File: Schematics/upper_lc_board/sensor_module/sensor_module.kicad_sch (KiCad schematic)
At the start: 30 parts, among them J2 HAL_SENS, J3 PT, J4 PT2, J7 TC, U7 ADC_ADS131M04IPWR, U9 OA-TLV9001IDCK

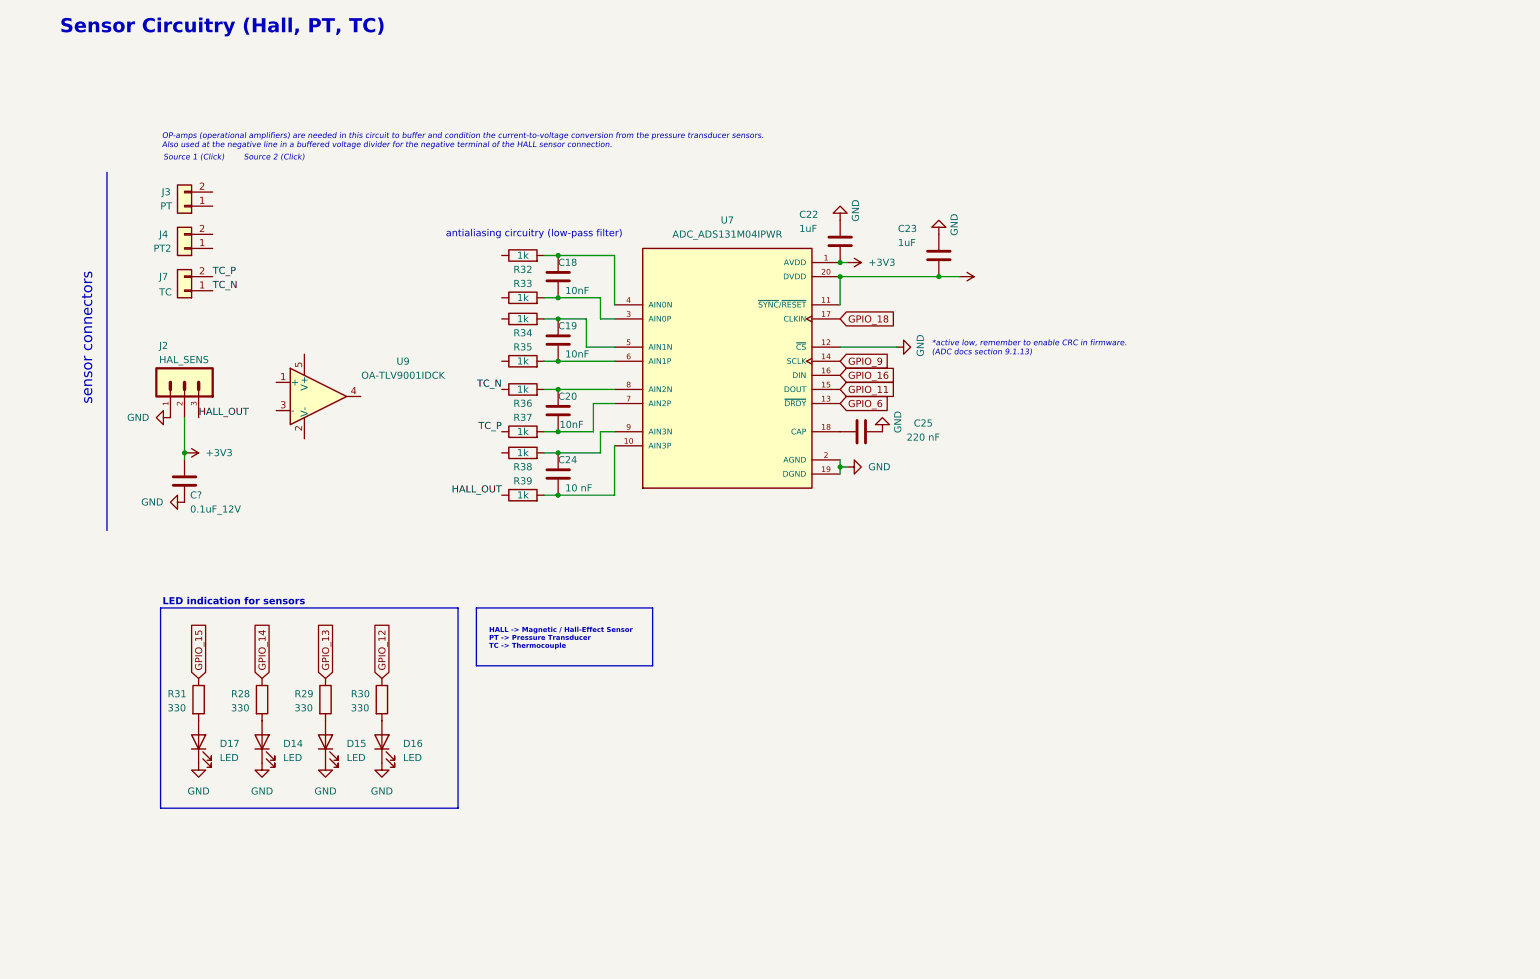
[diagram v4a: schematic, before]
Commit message: update sensor circuitry; implement reccomended pre-ADC circuitry
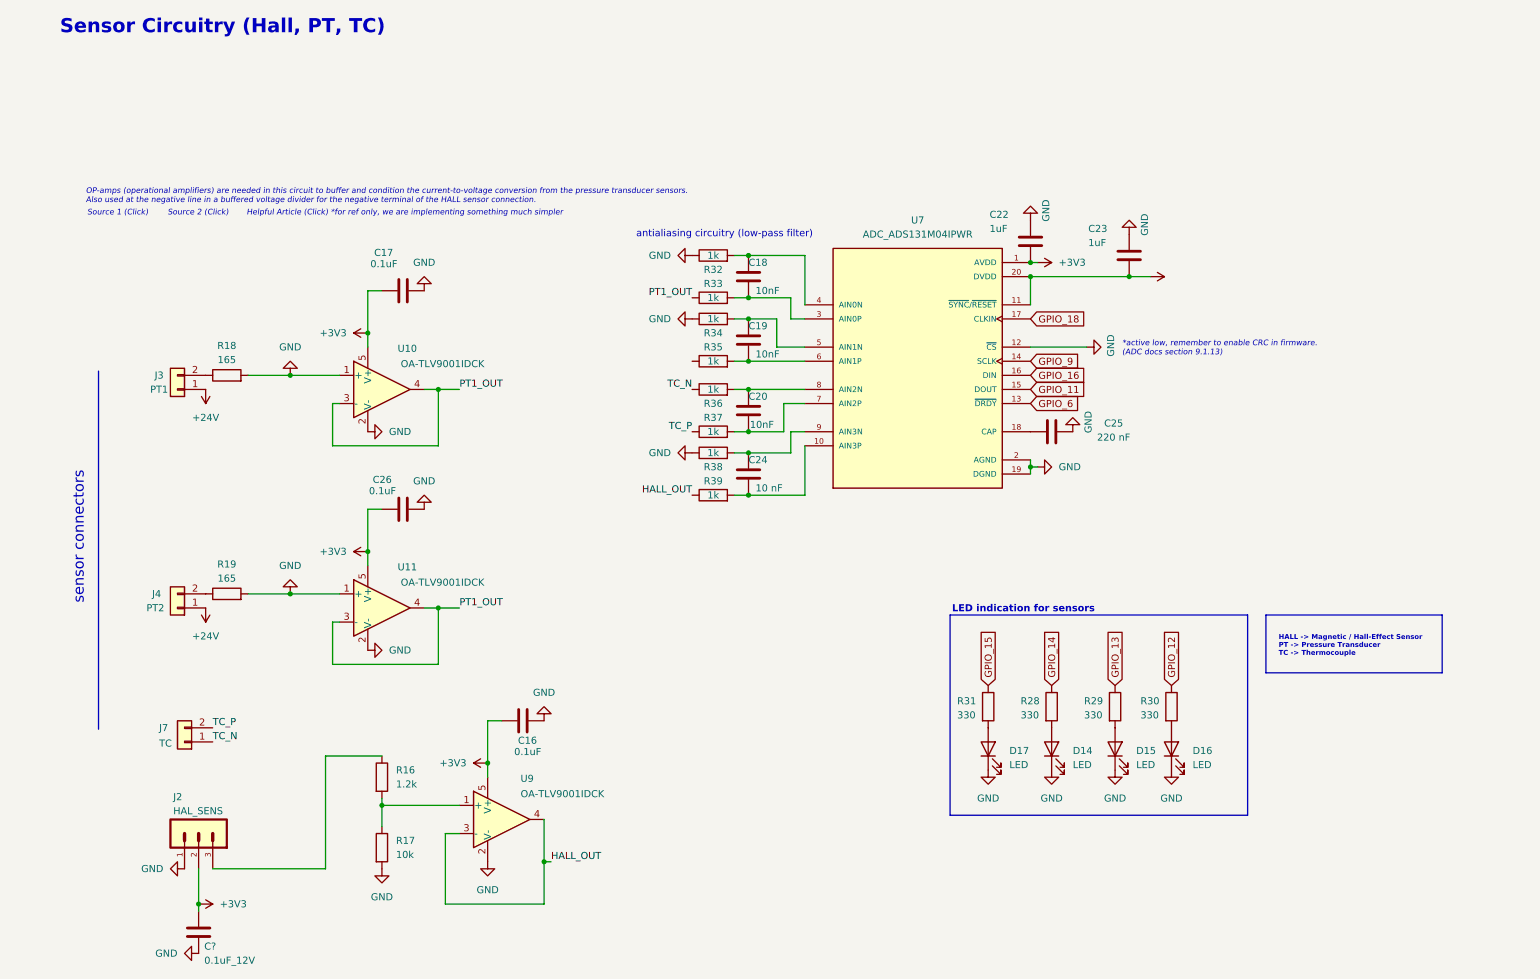
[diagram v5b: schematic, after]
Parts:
- added C16, C17, C26: 0.1uF, symbol Device:C
- added R16: 1.2k, symbol Device:R
- added R17: 10k, symbol Device:R
- added R18, R19: 165, symbol Device:R
- added U10, U11: OA-TLV9001IDCK, Package_TO_SOT_SMD:SOT-353_SC-70-5, symbol Amplifier_Operational:TLV9001IDCK
- J3: value PT -> PT1
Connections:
- net +3V3: now also U9.5 (V+), C16.1, C17.1, C26.1, U10.5 (V+), U11.5 (V+)
- net GND: now also R32.1, R34.1, R38.1, U9.2 (V-), C16.2, C17.2, C26.2, R17.2, R18.2, R19.2, U10.1 (+), U10.2 (V-), U11.1 (+), U11.2 (V-)
- net HALL_OUT: now also U9.3 (-), U9.4; no longer J2.3
- net +24V: now reaches J4.1 (Pin_1)
- net +24V: now also J3.1 (Pin_1)
- net at J4.2 (Pin_2): now also R19.1
- net at J3.2 (Pin_2): now also R18.1
- net at U9.1 (+): now also R16.2, R17.1
- net PT1_OUT: now reaches R33.1
- net PT1_OUT: now also U10.3 (-), U10.4, U11.3 (-), U11.4
- new net: J2.3, R16.1
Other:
- note added: "Helpful Article (Click) *for ref only, we are implementing something much simpler"
- moved on the sheet: C18, C19, C20, C22, C23, C24, C25, C?, D14, D15, D16, D17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

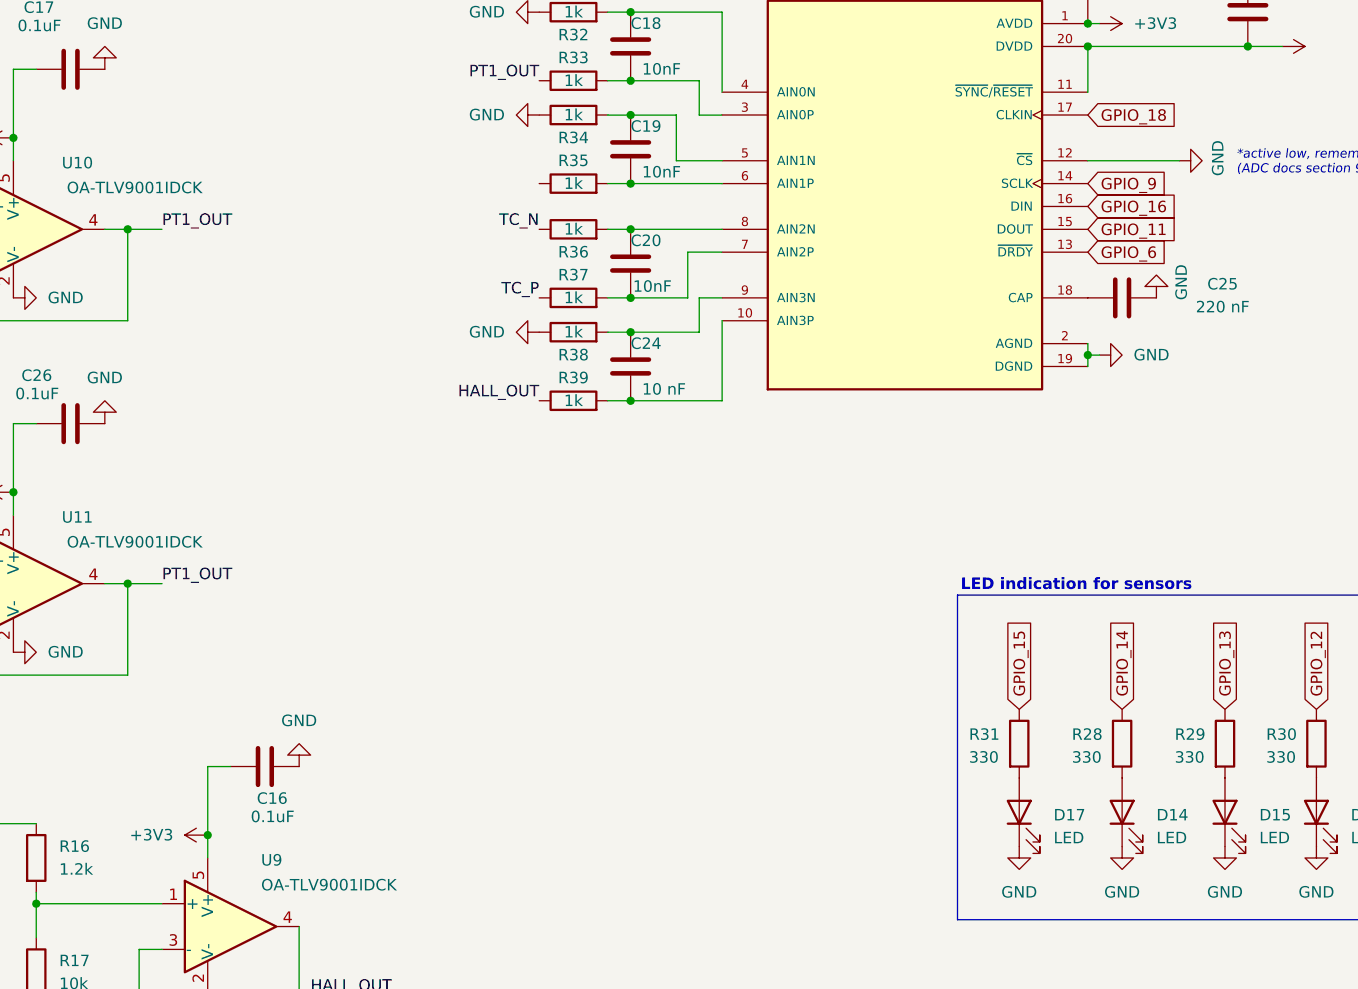
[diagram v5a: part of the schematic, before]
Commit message: update power circuitry (replaced OR-ing setup with a single power mux IC)
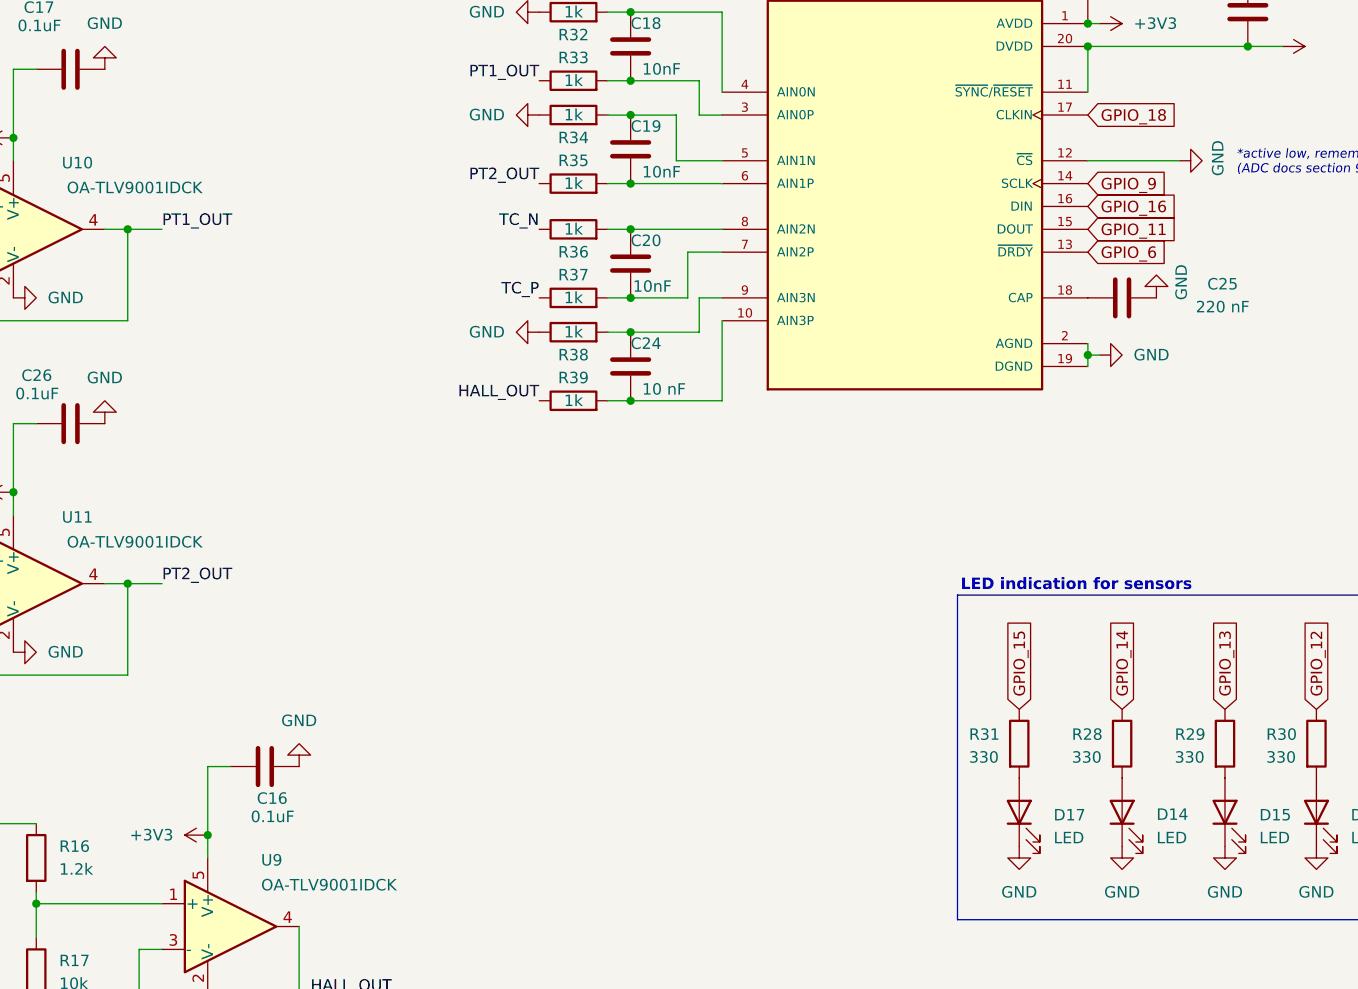
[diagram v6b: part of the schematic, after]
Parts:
- C16, C17, C18, C19, C20, C24, C26: footprint (none) -> Capacitor_SMD:C_0603_1608Metric
- R32, R33, R34, R35, R36, R37, R38, R39: footprint (none) -> Capacitor_SMD:C_0402_1005Metric
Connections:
- net PT1_OUT: no longer U11.3 (-), U11.4
- net PT2_OUT: now reaches R35.1
- net PT2_OUT: now also U11.3 (-), U11.4
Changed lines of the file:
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@@
 		)
 	)
+	(label "PT2_OUT"
+		(at 130.81 80.01 180)
+		(fields_autoplaced yes)
+		(effects
+			(font
+				(size 1.27 1.27)
+			)
+			(justify right bottom)
+		)
+	)
 	(label "PT1_OUT"
 		(at 130.81 68.58 180)
@@
 		)
 	)
-	(label "PT1_OUT"
+	(label "PT2_OUT"
 		(at 88.9 124.46 0)
 		(fields_autoplaced yes)
@@
 			)
 		)
-		(property "Footprint" ""
+		(property "Footprint" "Capacitor_SMD:C_0402_1005Metric"
 			(at 134.62 94.488 90)
 			(effects
@@
 			)
 		)
-		(property "Footprint" ""
+		(property "Footprint" "Capacitor_SMD:C_0402_1005Metric"
 			(at 134.62 81.788 90)
 			(effects
@@
 			)
 		)
-		(property "Footprint" ""
+		(property "Footprint" "Capacitor_SMD:C_0603_1608Metric"
 			(at 82.55 66.3448 0)
 			(effects
@@
 			)
 		)
-		(property "Footprint" ""
+		(property "Footprint" "Capacitor_SMD:C_0402_1005Metric"
 			(at 134.62 86.868 90)
 			(effects
@@
 			)
 		)
-		(property "Footprint" ""
+		(property "Footprint" "Capacitor_SMD:C_0603_1608Metric"
 			(at 141.9352 92.71 0)
 			(effects
@@
 		(on_board yes)
 		(dnp no)
-		(fields_autoplaced yes)
 		(property "Reference" "D14"
-			(at 199.39 150.1774 90)
+			(at 199.39 150.114 90)
 			(effects
 				(font
@@
 			)
 		)
-		(property "Footprint" ""
+		(property "Footprint" "Capacitor_SMD:C_0603_1608Metric"
 			(at 141.9352 80.01 0)
 			(effects
@@
 			)
 		)
-		(property "Footprint" ""
+		(property "Footprint" "Capacitor_SMD:C_0402_1005Metric"
 			(at 134.62 105.918 90)
 			(effects
@@
 			)
 		)
-		(property "Footprint" ""
+		(property "Footprint" "Capacitor_SMD:C_0603_1608Metric"
 			(at 82.55 105.7148 0)
 			(effects
@@
 			)
 		)
-		(property "Datasheet" "https://www.instrumart.com/assets/Setra-209H-Datasheet.pdf?srsltid=AfmBOopu2crXxkUQG31K4d3R_HBIXk4e909zcQpueoXf2bMSBoYDKgm2"
+		(property "Datasheet" ""
 			(at 39.37 148.59 0)
 			(effects
@@
 			)
 		)
-		(property "Description" "Pressure Transducer"
+		(property "Description" "Thermocouple"
 			(at 39.37 148.59 0)
 			(effects
@@
 			)
 		)
-		(property "Footprint" ""
+		(property "Footprint" "Capacitor_SMD:C_0402_1005Metric"
 			(at 134.62 70.358 90)
 			(effects
@@
 			)
 		)
-		(property "Footprint" ""
+		(property "Footprint" "Capacitor_SMD:C_0402_1005Metric"
 			(at 134.62 74.168 90)
 			(effects
@@
 			)
 		)
-		(property "Footprint" ""
+		(property "Footprint" "Capacitor_SMD:C_0402_1005Metric"
 			(at 134.62 98.298 90)
 			(effects
@@
 			)
 		)
-		(property "Footprint" ""
+		(property "Footprint" "Capacitor_SMD:C_0402_1005Metric"
 			(at 134.62 62.738 90)
 			(effects
@@
 			)
 		)
-		(property "Footprint" ""
+		(property "Footprint" "Capacitor_SMD:C_0603_1608Metric"
 			(at 104.14 143.8148 0)
 			(effects
@@
 			)
 		)
-		(property "Footprint" ""
+		(property "Footprint" "Capacitor_SMD:C_0603_1608Metric"
 			(at 141.9352 104.14 0)
 			(effects
@@
 			)
 		)
-		(property "Footprint" ""
+		(property "Footprint" "Capacitor_SMD:C_0603_1608Metric"
 			(at 141.9352 68.58 0)
 			(effects

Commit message: reviewing schematics
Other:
- note added: "*active low, remember to enable CRC in firmware. (ADC docs section 9.1.3)"
- note removed: "*active low, remember to enable CRC in firmware. (ADC docs section 9.1.13)"
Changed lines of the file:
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@@
 	)
 	(junction
+		(at 205.74 64.77)
+		(diameter 0)
+		(color 0 0 0 0)
+	)
+	(junction
 		(at 140.97 72.39)
 		(diameter 0)
@@
 	(wire
 		(pts
+			(xy 205.74 64.77) (xy 209.55 64.77)
+		)
+		(stroke
+			(width 0)
+			(type default)
+		)
+	)
+	(wire
+		(pts
 			(xy 146.05 77.47) (xy 151.13 77.47)
 		)
@@
 	(wire
 		(pts
-			(xy 191.77 64.77) (xy 209.55 64.77)
+			(xy 191.77 64.77) (xy 205.74 64.77)
 		)
 		(stroke
@@
 		)
 	)
-	(text "*active low, remember to enable CRC in firmware.\n(ADC docs section 9.1.13)"
+	(text "*active low, remember to enable CRC in firmware.\n(ADC docs section 9.1.3)"
 		(exclude_from_sim no)
 		(at 208.28 77.724 0)
@@
 					(unit 1)
 				)
+			)
+		)
+	)
+	(symbol
+		(lib_id "power:+3V3")
+		(at 205.74 64.77 180)
+		(unit 1)
+		(exclude_from_sim no)
+		(in_bom yes)
+		(on_board yes)
+		(dnp no)
+		(fields_autoplaced yes)
+		(property "Reference" "#PWR0101"
+			(at 205.74 60.96 0)
+			(effects
+				(font
+					(size 1.27 1.27)
+				)
+				(hide yes)
+			)
+		)
+		(property "Value" "+3V3"
+			(at 205.74 69.85 0)
+			(effects
+				(font
+					(size 1.27 1.27)
+				)
+			)
+		)
+		(property "Footprint" ""
+			(at 205.74 64.77 0)
+			(effects
+				(font
+					(size 1.27 1.27)
+				)
+				(hide yes)
+			)
+		)
+		(property "Datasheet" ""
+			(at 205.74 64.77 0)
+			(effects
+				(font
+					(size 1.27 1.27)
+				)
+				(hide yes)
+			)
+		)
+		(property "Description" "Power symbol creates a global label with name \"+3V3\""
+			(at 205.74 64.77 0)
+			(effects
+				(font
+					(size 1.27 1.27)
+				)
+				(hide yes)
+			)
+		)
+		(pin "1"
+		)
+		(instances
+			(project "upper_lc_board"
+				(path "/9b1a1d2a-fad7-4f10-83f3-1f83e9656c75/03f1622b-3dda-4e29-911f-7cc762ec6c20"
+					(reference "#PWR0101")
+					(unit 1)
+				)
